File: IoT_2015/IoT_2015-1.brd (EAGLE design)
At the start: 30 x 20 mm, 28 parts, among them Y1 ABLS-16.000MHZ-B4-T

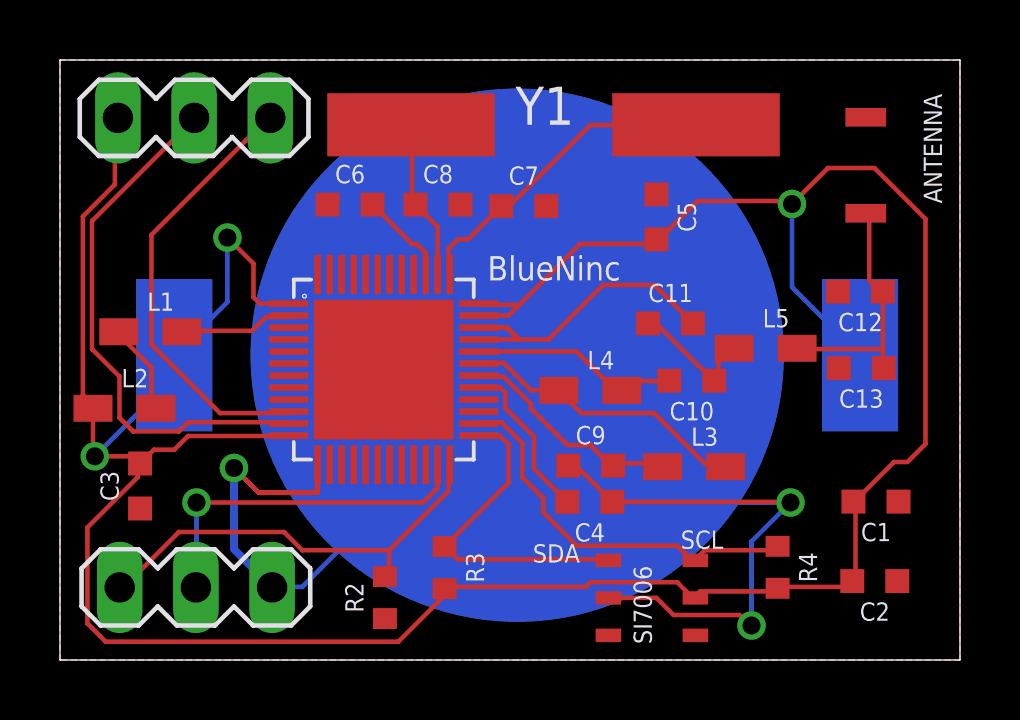
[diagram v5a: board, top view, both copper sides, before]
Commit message: Updated design with GND bottom layer
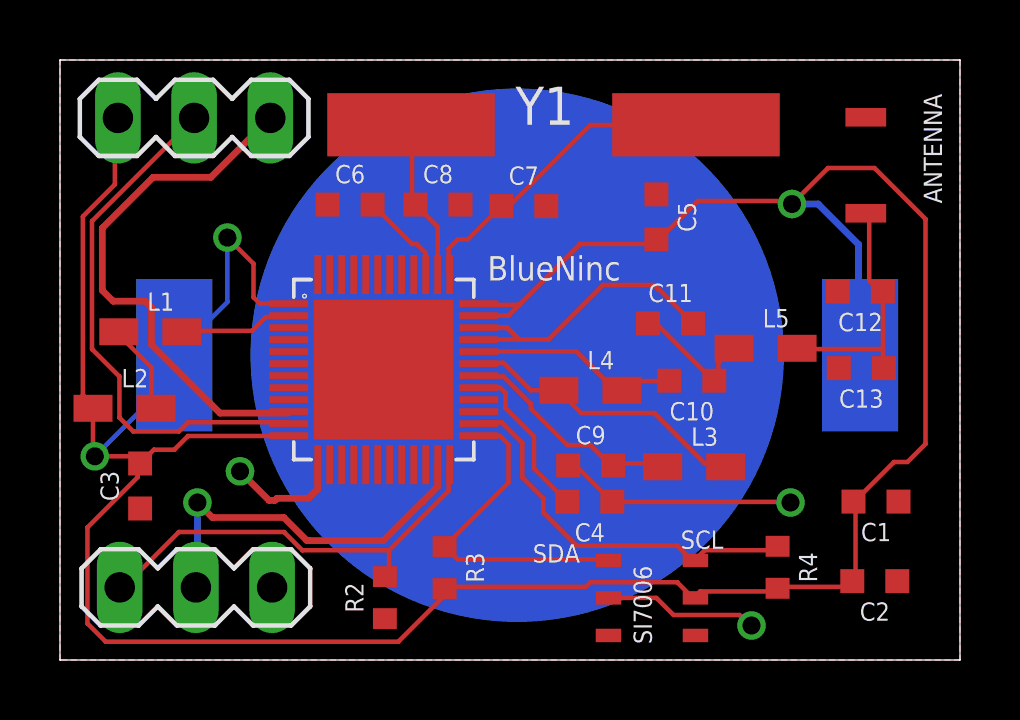
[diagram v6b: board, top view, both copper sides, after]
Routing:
- net GND: track 58.9 -> 27.0 mm
- net N$29: track 4.10 -> 0.00 mm
- net P0.06: track 14.8 -> 18.1 mm
- net SWDIO/NRESET: track 11.9 -> 12.9 mm
- net VDD: track 104.0 -> 104.5 mm
- added copper zone on layer 16, net GND
- removed copper zone on layer 16, net N$17
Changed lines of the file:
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@@
 <?xml version="1.0" encoding="utf-8"?>
 <!DOCTYPE eagle SYSTEM "eagle.dtd">
-<eagle version="7.2.0">
+<eagle version="7.3.0">
 <drawing>
 <settings>
@@
 <wire x1="25.6" y1="16.4" x2="24.4" y2="15.2" width="0.1524" layer="1"/>
 <via x="24.4" y="15.2" extent="1-16" drill="0.6"/>
-<wire x1="24.4" y1="15.2" x2="24.4" y2="12.43" width="0.1524" layer="16"/>
-<wire x1="24.4" y1="12.43" x2="26.67" y2="10.16" width="0.1524" layer="16"/>
 <wire x1="19.9644" y1="13.8684" x2="19.9644" y2="14.0144" width="0.1524" layer="1"/>
 <wire x1="19.9644" y1="14.0144" x2="21.25" y2="15.3" width="0.1524" layer="1"/>
@@
 <wire x1="1.1" y1="8.39" x2="1.1" y2="6.85" width="0.1524" layer="1"/>
 <wire x1="1.1" y1="6.85" x2="1.16" y2="6.79" width="0.1524" layer="1"/>
+<wire x1="24.4" y1="15.2" x2="25.27" y2="15.2" width="0.225" layer="16"/>
+<wire x1="25.27" y1="15.2" x2="26.62" y2="13.85" width="0.225" layer="16"/>
+<wire x1="26.62" y1="13.85" x2="26.62" y2="10.21" width="0.225" layer="16"/>
+<wire x1="26.62" y1="10.21" x2="26.67" y2="10.16" width="0.225" layer="16"/>
 </signal>
 <signal name="N$1">
@@
 <vertex x="30" y="0"/>
 </polygon>
-<wire x1="8.0772" y1="2.4384" x2="7.1628" y2="2.4384" width="0.1524" layer="16"/>
-<wire x1="15.24" y1="9.6012" x2="15.1194" y2="9.4806" width="0.1524" layer="16"/>
-<wire x1="15.1194" y1="9.4806" x2="8.0772" y2="2.4384" width="0.1524" layer="16"/>
-<wire x1="15.24" y1="10.16" x2="15.24" y2="9.6012" width="0.1524" layer="16"/>
-<wire x1="7.1628" y1="2.4384" x2="7.07" y2="2.42" width="0.1524" layer="16"/>
-<via x="5.8" y="6.4" extent="1-16" drill="0.6"/>
-<wire x1="5.8" y1="6.4" x2="5.8" y2="3.69" width="0.254" layer="16"/>
-<wire x1="5.8" y1="3.69" x2="7.07" y2="2.42" width="0.254" layer="16"/>
 <wire x1="16.94" y1="6.48" x2="17.2" y2="6.48" width="0.1524" layer="1"/>
 <wire x1="17.2" y1="6.48" x2="18.41" y2="5.27" width="0.1524" layer="1"/>
@@
 <wire x1="24.33" y1="5.27" x2="24.35" y2="5.25" width="0.1524" layer="1"/>
 <via x="24.35" y="5.25" extent="1-16" drill="0.6"/>
-<wire x1="24.35" y1="5.25" x2="19.35" y2="5.25" width="0.1524" layer="16"/>
-<wire x1="19.35" y1="5.25" x2="15.1194" y2="9.4806" width="0.1524" layer="16"/>
 <wire x1="18.28" y1="2.07" x2="19.88" y2="2.07" width="0.1524" layer="1"/>
 <wire x1="19.88" y1="2.07" x2="20.45" y2="1.5" width="0.1524" layer="1"/>
@@
 <wire x1="22.75" y1="1.45" x2="23.05" y2="1.15" width="0.1524" layer="1"/>
 <via x="23.05" y="1.15" extent="1-16" drill="0.6"/>
-<wire x1="23.05" y1="1.15" x2="23.05" y2="3.95" width="0.1524" layer="16"/>
-<wire x1="23.05" y1="3.95" x2="24.35" y2="5.25" width="0.1524" layer="16"/>
 <wire x1="13.96" y1="10.68" x2="15.3" y2="10.68" width="0.1524" layer="1"/>
 <wire x1="15.3" y1="10.68" x2="16.28" y2="10.68" width="0.1524" layer="1"/>
@@
 <wire x1="13.96" y1="11.08" x2="14.9" y2="11.08" width="0.1524" layer="1"/>
 <wire x1="14.9" y1="11.08" x2="15.3" y2="10.68" width="0.1524" layer="1"/>
-<wire x1="8.59" y1="6.51" x2="8.59" y2="5.58" width="0.1524" layer="1"/>
-<wire x1="8.59" y1="5.58" x2="6.62" y2="5.58" width="0.1524" layer="1"/>
-<wire x1="6.62" y1="5.58" x2="5.8" y2="6.4" width="0.1524" layer="1"/>
+<polygon width="0.254" layer="16" spacing="0.05" isolate="0.254">
+<vertex x="0" y="0"/>
+<vertex x="0" y="20"/>
+<vertex x="30" y="20"/>
+<vertex x="30" y="0"/>
+</polygon>
+<wire x1="8.59" y1="6.51" x2="8.59" y2="5.7" width="0.225" layer="1"/>
+<wire x1="8.59" y1="5.7" x2="8.28" y2="5.39" width="0.225" layer="1"/>
+<wire x1="8.28" y1="5.39" x2="7.23" y2="5.39" width="0.225" layer="1"/>
+<wire x1="7.23" y1="5.39" x2="7.16" y2="5.32" width="0.225" layer="1"/>
+<wire x1="7.16" y1="5.32" x2="6.97" y2="5.32" width="0.225" layer="1"/>
+<wire x1="6.97" y1="5.32" x2="6" y2="6.29" width="0.225" layer="1"/>
+<via x="6" y="6.29" extent="1-16" drill="0.6"/>
 </signal>
 <signal name="N$3">
@@
 <contactref element="U$1" pad="10"/>
 <contactref element="P67VDD" pad="1"/>
-<wire x1="5.334" y1="8.2296" x2="7.62" y2="8.2296" width="0.1524" layer="1"/>
-<wire x1="3.048" y1="10.5156" x2="5.334" y2="8.2296" width="0.1524" layer="1"/>
-<wire x1="3.048" y1="14.1732" x2="3.048" y2="10.5156" width="0.1524" layer="1"/>
-<wire x1="6.858" y1="17.9832" x2="3.048" y2="14.1732" width="0.1524" layer="1"/>
 <wire x1="7.62" y1="8.2296" x2="7.62" y2="8.28" width="0.1524" layer="1"/>
 <wire x1="6.858" y1="17.9832" x2="7.01" y2="18.07" width="0.1524" layer="1"/>
+<wire x1="3.048" y1="10.5156" x2="3.048" y2="11.752" width="0.225" layer="1"/>
+<wire x1="3.048" y1="11.752" x2="2.84" y2="11.96" width="0.225" layer="1"/>
+<wire x1="2.84" y1="11.96" x2="1.77" y2="11.96" width="0.225" layer="1"/>
+<wire x1="1.77" y1="11.96" x2="1.41" y2="12.32" width="0.225" layer="1"/>
+<wire x1="1.41" y1="12.32" x2="1.41" y2="14.4" width="0.225" layer="1"/>
+<wire x1="1.41" y1="14.4" x2="3.1" y2="16.09" width="0.225" layer="1"/>
+<wire x1="3.1" y1="16.09" x2="5.03" y2="16.09" width="0.225" layer="1"/>
+<wire x1="5.03" y1="16.09" x2="7.01" y2="18.07" width="0.225" layer="1"/>
+<wire x1="7.62" y1="8.2296" x2="5.334" y2="8.2296" width="0.225" layer="1"/>
+<wire x1="5.334" y1="8.2296" x2="3.048" y2="10.5156" width="0.225" layer="1"/>
 </signal>
 <signal name="P0.07">
@@
 <contactref element="U$1" pad="23"/>
 <contactref element="JTAG" pad="2"/>
-<wire x1="12.59" y1="6.51" x2="12.59" y2="5.74" width="0.1524" layer="1"/>
-<wire x1="12.59" y1="5.74" x2="12.1" y2="5.25" width="0.1524" layer="1"/>
-<wire x1="12.1" y1="5.25" x2="4.55" y2="5.25" width="0.1524" layer="1"/>
-<via x="4.55" y="5.25" extent="1-16" drill="0.6"/>
-<wire x1="4.55" y1="5.25" x2="4.55" y2="2.44" width="0.1524" layer="16"/>
-<wire x1="4.55" y1="2.44" x2="4.53" y2="2.42" width="0.1524" layer="16"/>
+<wire x1="12.59" y1="6.51" x2="12.59" y2="5.78" width="0.225" layer="1"/>
+<wire x1="12.59" y1="5.78" x2="12.08" y2="5.27" width="0.225" layer="1"/>
+<wire x1="12.08" y1="5.27" x2="12.07" y2="5.27" width="0.225" layer="1"/>
+<wire x1="12.07" y1="5.27" x2="10.78" y2="3.98" width="0.225" layer="1"/>
+<wire x1="10.78" y1="3.98" x2="8.29" y2="3.98" width="0.225" layer="1"/>
+<wire x1="8.29" y1="3.98" x2="8.28" y2="3.99" width="0.225" layer="1"/>
+<wire x1="8.28" y1="3.99" x2="8.22" y2="3.99" width="0.225" layer="1"/>
+<wire x1="8.22" y1="3.99" x2="7.46" y2="4.75" width="0.225" layer="1"/>
+<wire x1="7.46" y1="4.75" x2="5.08" y2="4.75" width="0.225" layer="1"/>
+<wire x1="5.08" y1="4.75" x2="4.58" y2="5.25" width="0.225" layer="1"/>
+<via x="4.58" y="5.25" extent="1-16" drill="0.6"/>
+<wire x1="4.58" y1="5.25" x2="4.58" y2="2.47" width="0.225" layer="16"/>
+<wire x1="4.58" y1="2.47" x2="4.53" y2="2.42" width="0.225" layer="16"/>
 </signal>
 <signal name="SWDCLK">
@@
 <signal name="N$43">
 </signal>
-<signal name="N$17">
-<polygon width="0.254" layer="16" spacing="0.05" isolate="0.254">
-<vertex x="0" y="0"/>
-<vertex x="0" y="20"/>
-<vertex x="30" y="20"/>
-<vertex x="30" y="0"/>
-</polygon>
-</signal>
 <signal name="N$27">
 <wire x1="14.01" y1="11.07" x2="14.92" y2="11.07" width="0.1524" layer="1"/>
@@
 </signal>
 <signal name="N$29">
-<wire x1="8.58" y1="6.54" x2="8.58" y2="5.58" width="0.1524" layer="1"/>
-<wire x1="8.58" y1="5.58" x2="8.57" y2="5.57" width="0.1524" layer="1"/>
-<wire x1="8.57" y1="5.57" x2="6.63" y2="5.57" width="0.1524" layer="1"/>
-<wire x1="6.63" y1="5.57" x2="5.79" y2="6.41" width="0.1524" layer="1"/>
 </signal>
 </signals>

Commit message: Stop masks are corrected
All DRC errors are corrected. Specially the stop masks have been
corrected in the footprints of interest.
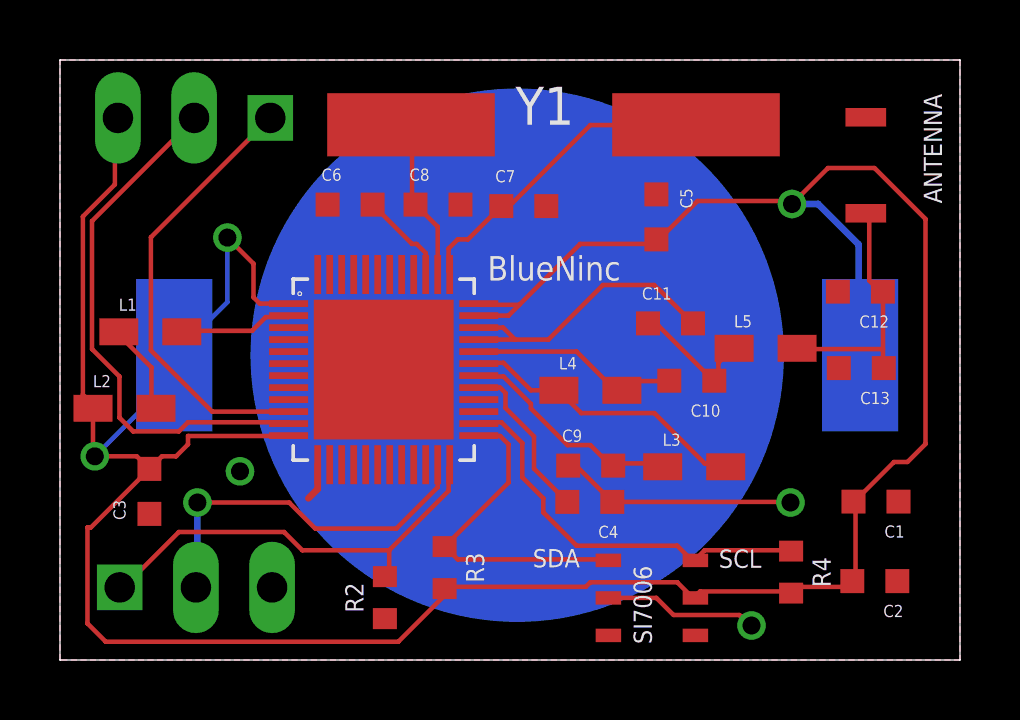
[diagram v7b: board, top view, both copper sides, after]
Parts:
- JTAG, P67VDD: device con-lstb:MA03-1 -> custom-con-lstb:MA03-1
- moved R4 0.48 mm to (24.4, 2.93)
- moved C3 0.36 mm to (2.98, 5.62)
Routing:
- net P0.06: track 18.1 -> 14.8 mm
- net GND: track 27.0 -> 24.1 mm
- net N$27: track 1.42 -> 0.00 mm
